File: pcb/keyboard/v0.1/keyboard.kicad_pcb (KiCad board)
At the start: 2 copper layers, 80 x 50 mm, 142 parts, among them J1 USB2.0, J2 SWD, SW1 BACKTICK, SW10 9, SW11 0, SW12 BACKSPACE, SW13 TAB, SW14 Q, SW15 W, SW16 E, SW17 R, SW18 T, SW19 Y, SW2 1, SW20 U, SW21 I, SW22 O, SW23 P, SW24 RETURN, SW25 CAPS, SW26 A, SW27 S, SW28 D, SW29 F, SW3 2, SW30 G, SW31 H, SW32 J, SW33 K, SW34 L, SW35 SEMI, SW36 QUOTE, SW37 LSHIFT, SW38 Z, SW39 X, SW4 3, SW40 C, SW41 V, SW42 B, SW43 N, SW44 M, SW45 COMMA, SW46 DOT, SW47 QUEST, SW48 RSHIFT, SW49 FN, SW5 4, SW50 LCTRL, SW51 LSUPER, SW52 LALT, SW53 SPACE, SW54 RALT, SW55 RSUPER, SW56 MENU, SW57 RCTRL, SW58 C1, SW59 C2, SW6 5, SW60 C3, SW61 C4, SW62 C5, SW63 C6, SW7 6, SW8 7, SW9 8, U1 MDBT50Q-P1MV2, Y1 32.768

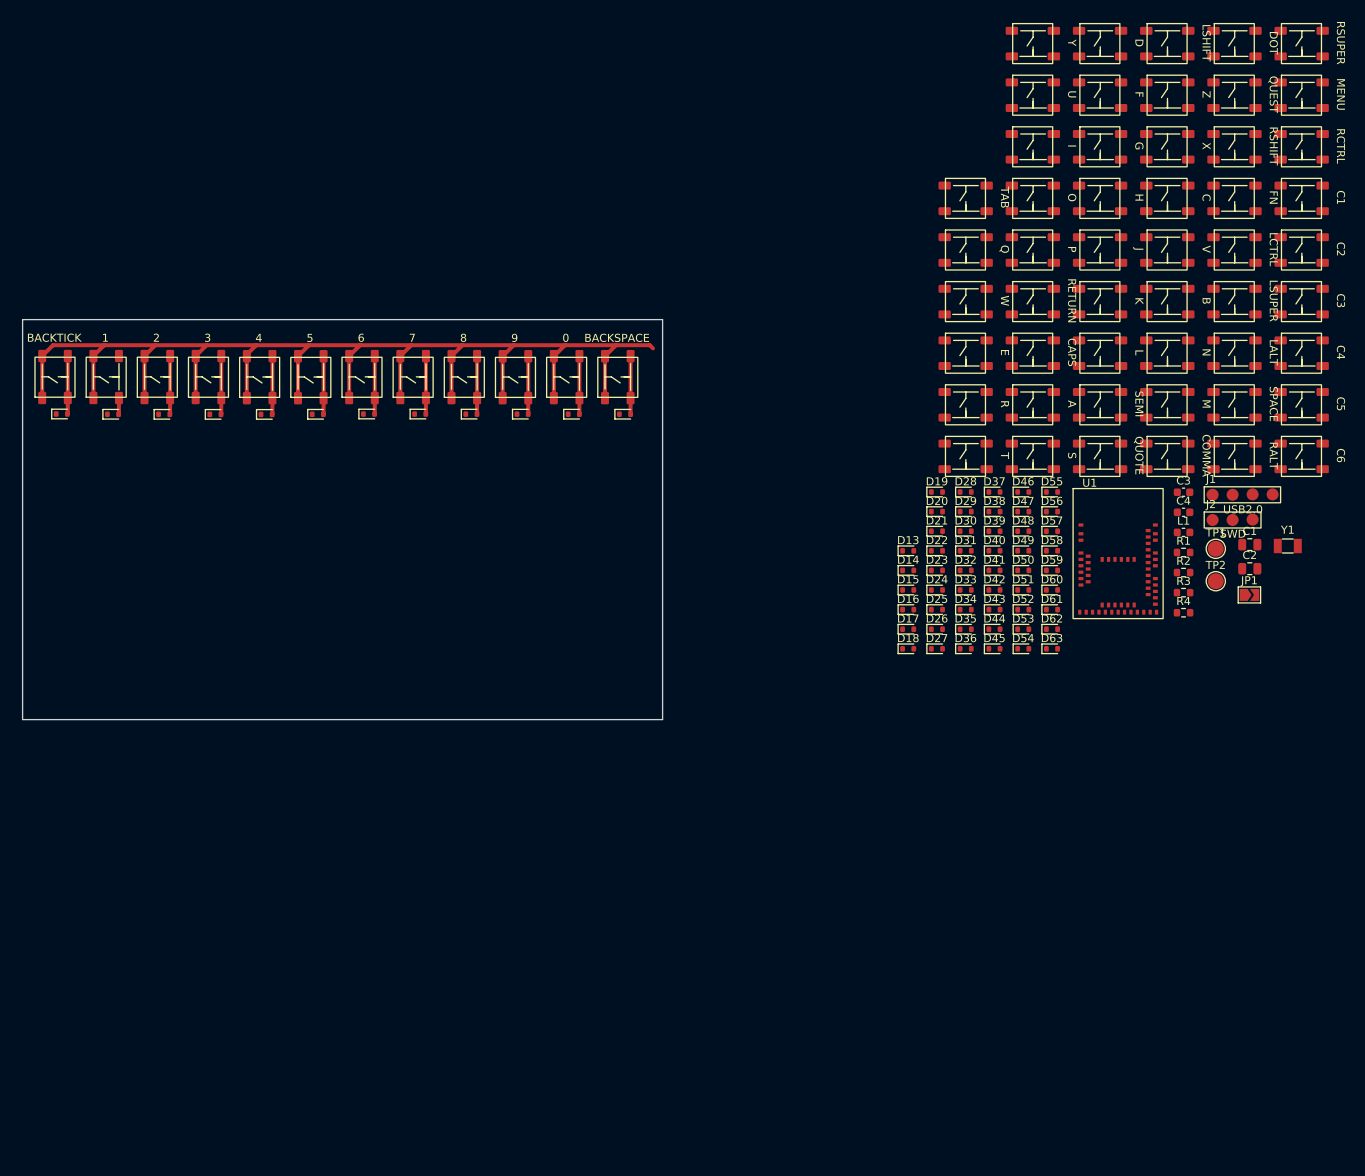
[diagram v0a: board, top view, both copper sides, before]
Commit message: Initial keys layout
Not sure if this is how we want it yet. Will have to test out without
the silkscreen key labels if it might give some more space
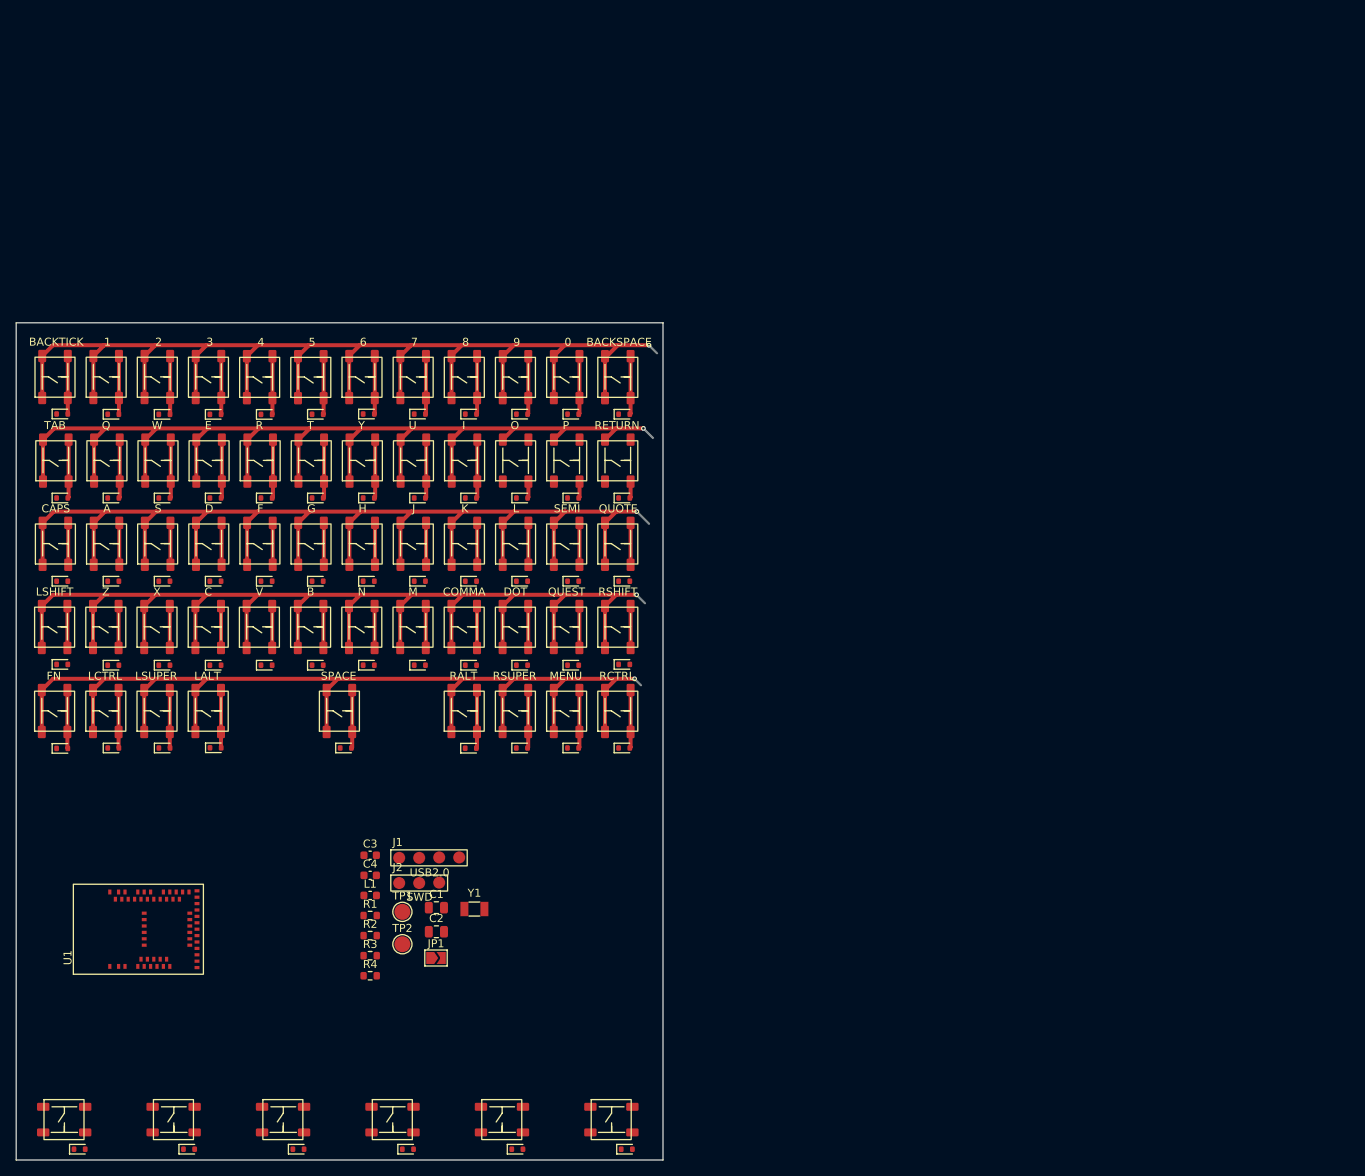
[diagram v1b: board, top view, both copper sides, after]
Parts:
- moved SW58 192.8 mm to (85.2, 189.6)
- moved SW59 178.0 mm to (98.9, 189.6)
- moved SW60 163.3 mm to (112.5, 189.6)
- moved SW49 161.6 mm to (85.0, 142.8), turned to 90 degrees
- moved SW37 158.2 mm to (85.0, 132.2), turned to 90 degrees
- moved SW50 153.1 mm to (91.4, 142.8), turned to 90 degrees
- moved SW38 149.4 mm to (91.4, 132.2), turned to 90 degrees
- moved SW61 148.6 mm to (126.2, 189.6)
- moved SW51 144.7 mm to (97.8, 142.8), turned to 90 degrees
- moved D58 142.7 mm to (89.7, 194.9)
- moved SW39 140.8 mm to (97.8, 132.2), turned to 90 degrees
- moved U1 138.9 mm to (88.9, 173.1), turned to 90 degrees
- moved SW52 136.3 mm to (104.2, 142.8), turned to 90 degrees
- moved SW62 134.1 mm to (139.9, 189.6)
- moved SW40 132.2 mm to (104.2, 132.2), turned to 90 degrees
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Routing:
- net /SOURCE3: track 0.00 -> 161.7 mm, vias 0 -> 1
- net /SOURCE4: track 0.00 -> 161.2 mm, vias 0 -> 1
- net /SOURCE2: track 0.00 -> 146.4 mm, vias 0 -> 1
- net /SOURCE5: track 0.00 -> 138.9 mm, vias 0 -> 1
- net Net-(D19-A): track 0.00 -> 7.34 mm
- net Net-(D14-A): track 0.00 -> 7.34 mm
- net Net-(D21-A): track 0.00 -> 7.34 mm
- net Net-(D20-A): track 0.00 -> 7.34 mm
- net Net-(D18-A): track 0.00 -> 7.34 mm
- net Net-(D17-A): track 0.00 -> 7.34 mm
- net Net-(D16-A): track 0.00 -> 7.34 mm
- net Net-(D15-A): track 0.00 -> 7.34 mm
- net Net-(D13-A): track 0.00 -> 7.34 mm
- net Net-(D49-A): track 0.00 -> 7.32 mm
- net Net-(D54-A): track 0.00 -> 7.31 mm
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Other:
- board size 80 x 50 mm -> 80.9 x 104.7 mm
